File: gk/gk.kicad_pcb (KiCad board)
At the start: 6 copper layers, 108 x 158.8 mm, 199 parts, among them J1 USB_C_Receptacle_USB2.0, J10 Barrel_Jack_Switch, J11 Conn_01x02, J2 Conn_01x02, J3 Conn_02x27_Top_Bottom, J4 Micro_SD_Card_Det2, J5 AudioJack3_SwitchTR, J6 Conn_01x02, J7 Conn_01x02, J8 Conn_ARM_JTAG_SWD_10, J9 Conn_01x06, SW1 SW_Push, SW2 SW_Push, SW3 RotaryEncoder_Switch, U1 WE-TVS-82400102, U10 MAX17048, U11 ULN2003A, U2 MCP73831-2-OT, U3 AP62300WU, U4 STM32H747BITx, U5 PT4110E89E, U6 IS42S16320F-7TLI-TR, U7 PCM1754DBQ, U8 PAM8008, U9 LSM6DSL, Y1 16MHz

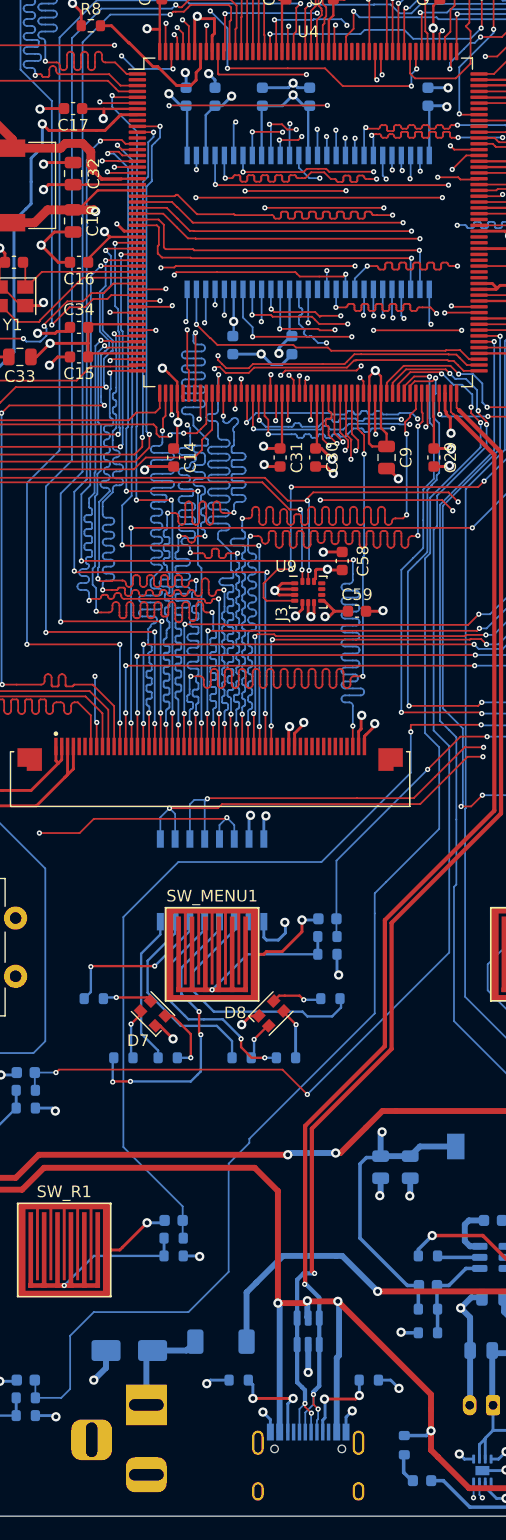
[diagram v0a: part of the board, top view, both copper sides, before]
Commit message: Add vbat_stat detection
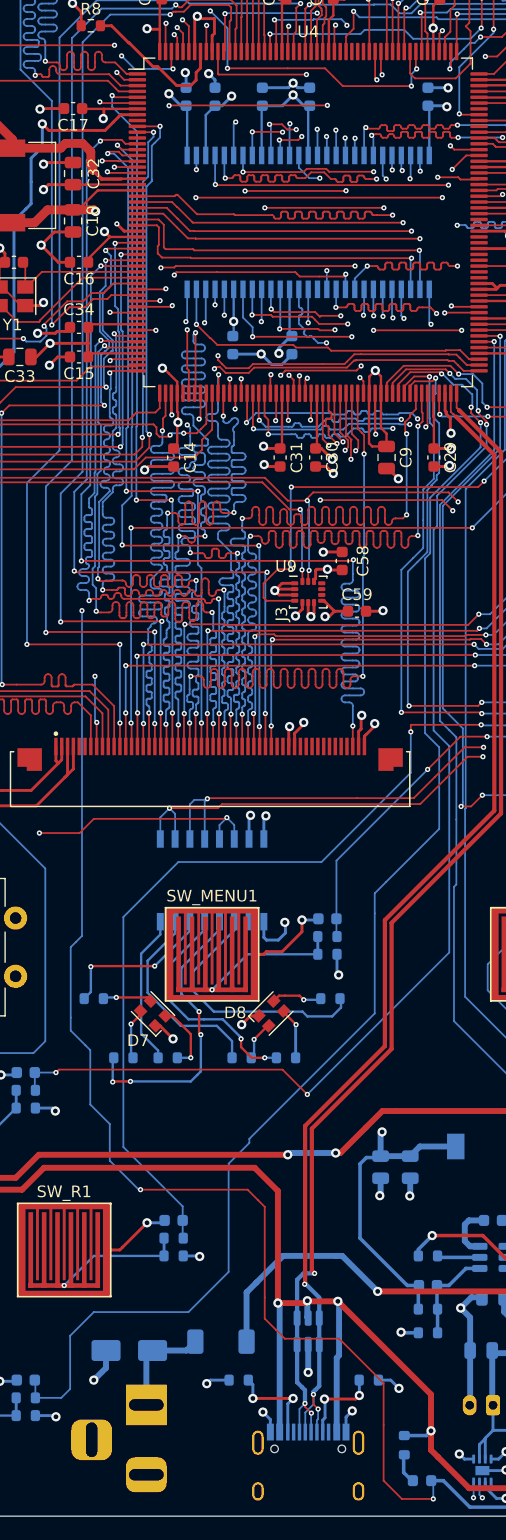
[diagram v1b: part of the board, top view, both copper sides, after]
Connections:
- D3 pad 1: Net-(D3-K) -> VBAT_STAT
- U2 pad 1: Net-(D3-K) -> VBAT_STAT
- U4 pad 2: unconnected-(U4-PE3-Pad2) -> VBAT_STAT
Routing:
- net VBAT_STAT: track 0.00 -> 174.2 mm, vias 0 -> 4
- net Net-(D3-K): track 22.7 -> 0.00 mm

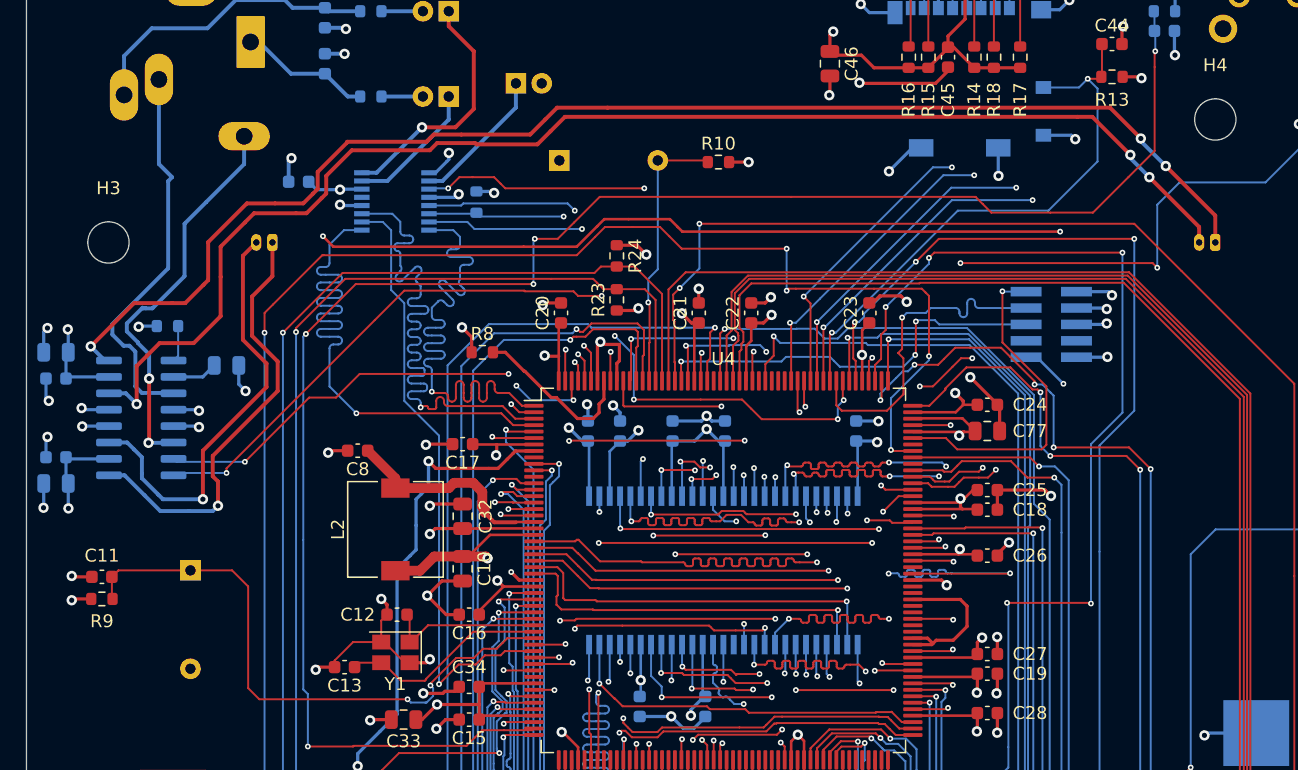
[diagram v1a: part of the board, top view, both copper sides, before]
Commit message: Switch speaker amplifier to mono
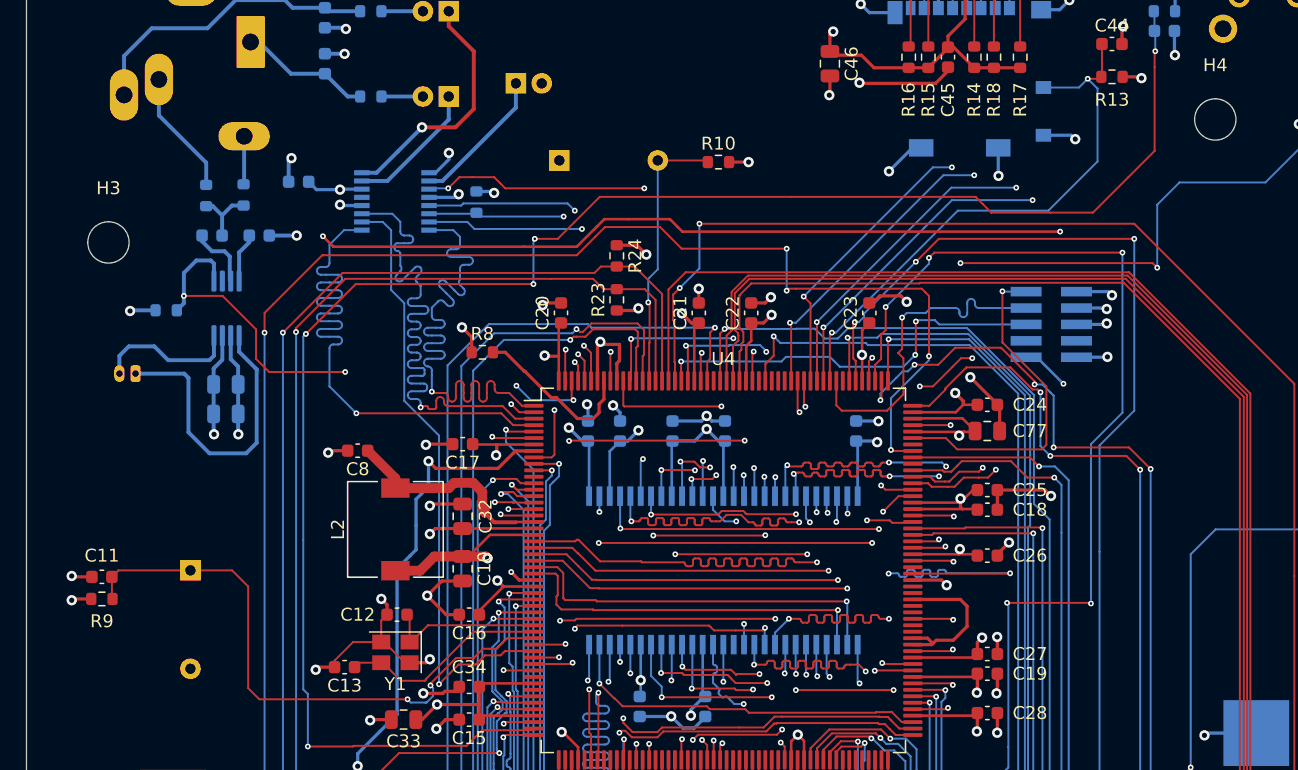
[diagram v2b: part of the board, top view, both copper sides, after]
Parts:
- removed C53, C54: 100n, Capacitor_SMD:C_0603_1608Metric
- removed C55, C56, C57: 1u, Capacitor_SMD:C_0805_2012Metric
- removed J7: Conn_01x02, Connector_Molex:Molex_PicoBlade_53048-0210_1x02_P1.25mm_Horizontal
- removed U8: PAM8008, Package_SO:SOP-16_3.9x9.9mm_P1.27mm
- added C80: 10u, Capacitor_SMD:C_0805_2012Metric, B.Cu at (59.9, 52.3)
- added C81: 1u, Capacitor_SMD:C_0805_2012Metric, B.Cu at (59.9, 54.6)
- added C82: 0.1u, Capacitor_SMD:C_0603_1608Metric, B.Cu at (58.8, 40.7)
- added C83: 0.1u, Capacitor_SMD:C_0603_1608Metric, B.Cu at (62.5, 40.7)
- added R64: 10k, Resistor_SMD:R_0603_1608Metric, B.Cu at (61.3, 37.6)
- added R65: 10k, Resistor_SMD:R_0603_1608Metric, B.Cu at (58.4, 37.6)
- added U12: PAM8302AAS, Package_SO:MSOP-8_3x3mm_P0.65mm, B.Cu at (59.9, 46.4)
- moved J6 14.7 mm to (52.9, 51.4)
- moved R22 1.22 mm to (55.3, 46.5)
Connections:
- U4 pad 164: SPKR_MUTE -> unconnected-(U4-PI3-Pad164)
- U4 pad 45: SPKR_VOLUME -> unconnected-(U4-PA0-Pad45)
- U4 pad 9: unconnected-(U4-PI8-Pad9) -> SPKR_NSD
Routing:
- net Net-(J7-Pin_1): track 104.8 -> 0.00 mm, vias 3 -> 0
- net Net-(J7-Pin_2): track 104.6 -> 0.00 mm, vias 3 -> 0
- net SPKR_MUTE: track 68.1 -> 0.00 mm, vias 6 -> 0
- net SPKR_VOLUME: track 58.9 -> 0.00 mm, vias 3 -> 0
- net SPKR_NSD: track 2.81 -> 46.4 mm, vias 0 -> 3
- net SPKRL: track 30.7 -> 3.73 mm, vias 2 -> 0
- net Net-(J6-Pin_2): track 33.2 -> 11.1 mm, vias 1 -> 0
- net SPKRR: track 30.3 -> 9.68 mm
- net Net-(J6-Pin_1): track 33.9 -> 23.6 mm, vias 1 -> 0
- net GND: track 424.1 -> 417.0 mm, vias 159 -> 152
- net VCC: track 331.2 -> 324.3 mm, vias 66 -> 65
- net Net-(C82-Pad2): track 0.00 -> 5.07 mm
- net Net-(U12-IN+): track 0.00 -> 5.01 mm
- net Net-(U12-IN-): track 0.00 -> 3.85 mm
- net Net-(U8-BYPASS): track 3.52 -> 0.00 mm
